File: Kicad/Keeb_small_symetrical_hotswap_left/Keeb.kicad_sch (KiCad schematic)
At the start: 28 parts, among them J1 TYPE-C-31-M-12, SW1 CherryMX, SW10 CherryMX, SW11 CherryMX, SW13 CherryMX, SW14 CherryMX, SW15 CherryMX, SW16 CherryMX, SW17 CherryMX, SW18 CherryMX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

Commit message: added encoder
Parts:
- added U2: KY-040, KY-040:KY-040-PORT, symbol KY-040:KY-040
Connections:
- net 28: now also U2.SW
- net 3: now also U2.DT
- net 3v3: now also J1.B5 (CC2), J1.B8 (SBU2), U2.VCC; no longer J1.A4_B9 (VBUS), J1.B4_A9 (VBUS)
- net 4: now also U2.CLK
- net GND: now also U2.GND
- net VSYS: now also J1.A4_B9 (VBUS), J1.B4_A9 (VBUS); no longer J1.B5 (CC2), J1.B8 (SBU2)

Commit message: Managed to add a button, optimised tracks, switched some connections around
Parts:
- added SW2: CherryMX, ScottoKeebs_Hotswap:Hotswap_MX_1.00u, symbol Keeb-rescue:CherryMX-CherryMX
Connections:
- net 0: no longer J1.A5 (CC1), J1.A8 (SBU1)
- net 1: now also SW2.2; no longer J1.A6 (DP1), J1.A7 (DN1)
- net 14: now also J1.A6 (DP1), J1.A7 (DN1)
- net 15: now also J1.B6 (DP2), J1.B7 (DN2)
- net 2: now also J1.A5 (CC1), J1.A8 (SBU1); no longer J1.B6 (DP2), J1.B7 (DN2)
- net 20: now also SW16.1; no longer SW15.2
- net 21: now also SW15.2; no longer SW19.1
- net 22: now also SW19.1; no longer SW20.1
- net 26: now also SW20.1; no longer SW16.1
- net GND: now also SW2.1
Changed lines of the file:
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@@
     (stroke (width 0) (type default))
   )
-  (global_label "26" (shape input) (at 146.05 97.79 270) (fields_autoplaced)
+  (global_label "20" (shape input) (at 146.05 97.79 270) (fields_autoplaced)
     (effects (font (size 1.27 1.27)) (justify right))
     (property "Intersheetrefs" "${INTERSHEET_REFS}" (at 146.05 102.54 90)
@@
     )
   )
-  (global_label "2" (shape input) (at 91.44 36.83 0) (fields_autoplaced)
-    (effects (font (size 1.27 1.27)) (justify left))
-    (property "Intersheetrefs" "${INTERSHEET_REFS}" (at 94.9805 36.83 0)
+  (global_label "15" (shape input) (at 91.44 36.83 0) (fields_autoplaced)
+    (effects (font (size 1.27 1.27)) (justify left))
+    (property "Intersheetrefs" "${INTERSHEET_REFS}" (at 96.19 36.83 0)
       (effects (font (size 1.27 1.27)) (justify left) hide)
     )
@@
     )
   )
-  (global_label "20" (shape input) (at 156.21 85.09 270) (fields_autoplaced)
+  (global_label "21" (shape input) (at 156.21 85.09 270) (fields_autoplaced)
     (effects (font (size 1.27 1.27)) (justify right))
     (property "Intersheetrefs" "${INTERSHEET_REFS}" (at 156.21 89.84 90)
@@
     )
   )
-  (global_label "1" (shape input) (at 48.26 36.83 180) (fields_autoplaced)
-    (effects (font (size 1.27 1.27)) (justify right))
-    (property "Intersheetrefs" "${INTERSHEET_REFS}" (at 44.7195 36.83 0)
+  (global_label "14" (shape input) (at 48.26 36.83 180) (fields_autoplaced)
+    (effects (font (size 1.27 1.27)) (justify right))
+    (property "Intersheetrefs" "${INTERSHEET_REFS}" (at 43.51 36.83 0)
       (effects (font (size 1.27 1.27)) (justify right) hide)
     )
@@
     )
   )
+  (global_label "GND" (shape input) (at 118.11 97.79 270) (fields_autoplaced)
+    (effects (font (size 1.27 1.27)) (justify right))
+    (property "Intersheetrefs" "${INTERSHEET_REFS}" (at 118.11 103.9915 90)
+      (effects (font (size 1.27 1.27)) (justify right) hide)
+    )
+  )
   (global_label "18" (shape input) (at 156.21 72.39 270) (fields_autoplaced)
     (effects (font (size 1.27 1.27)) (justify right))
@@
     )
   )
-  (global_label "21" (shape input) (at 158.75 85.09 270) (fields_autoplaced)
+  (global_label "22" (shape input) (at 158.75 85.09 270) (fields_autoplaced)
     (effects (font (size 1.27 1.27)) (justify right))
     (property "Intersheetrefs" "${INTERSHEET_REFS}" (at 158.75 89.84 90)
@@
     )
   )
+  (global_label "1" (shape input) (at 128.27 97.79 270) (fields_autoplaced)
+    (effects (font (size 1.27 1.27)) (justify right))
+    (property "Intersheetrefs" "${INTERSHEET_REFS}" (at 128.27 101.3305 90)
+      (effects (font (size 1.27 1.27)) (justify right) hide)
+    )
+  )
   (global_label "19" (shape input) (at 85.09 119.38 0) (fields_autoplaced)
     (effects (font (size 1.27 1.27)) (justify left))
@@
     )
   )
-  (global_label "22" (shape input) (at 158.75 97.79 90) (fields_autoplaced)
+  (global_label "26" (shape input) (at 158.75 97.79 90) (fields_autoplaced)
     (effects (font (size 1.27 1.27)) (justify left))
     (property "Intersheetrefs" "${INTERSHEET_REFS}" (at 158.75 93.04 90)
@@
     )
   )
-  (global_label "0" (shape input) (at 44.45 34.29 180) (fields_autoplaced)
+  (global_label "2" (shape input) (at 44.45 34.29 180) (fields_autoplaced)
     (effects (font (size 1.27 1.27)) (justify right))
     (property "Intersheetrefs" "${INTERSHEET_REFS}" (at 40.9095 34.29 0)
@@
         )
       )
+    )
+  )
+  (symbol (lib_id "Keeb-rescue:CherryMX-CherryMX") (at 123.19 97.79 0) (unit 1)
+    (in_bom yes) (on_board yes) (dnp no)
+    (property "Reference" "SW2" (at 123.19 90.551 0)
+      (effects (font (size 1.27 1.27)))
+    )
+    (property "Value" "CherryMX" (at 123.19 92.8624 0)
+      (effects (font (size 1.27 1.27)))
+    )
+    (property "Footprint" "ScottoKeebs_Hotswap:Hotswap_MX_1.00u" (at 123.19 97.155 0)
+      (effects (font (size 1.27 1.27)) hide)
+    )
+    (property "Datasheet" "" (at 123.19 97.155 0)
+      (effects (font (size 1.27 1.27)) hide)
+    )
+    (pin "1")
+    (pin "2")
+    (instances
+      (project "Keeb"
+        (path "/f8892ba2-997e-41dc-a7e4-c2b6962ff100"
+          (reference "SW2") (unit 1)
+        )
+      )

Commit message: Updated a PiPico footprint
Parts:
- U1: footprint MCU_RaspberryPi_and_Boards:RPi_Pico_SMD_TH_NO_HOLES -> MCU_RaspberryPi_and_Boards:RPi_Pico_SMD_TH_NO_BACK_HOLES
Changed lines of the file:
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@@
       (effects (font (size 1.27 1.27)))
     )
-    (property "Footprint" "MCU_RaspberryPi_and_Boards:RPi_Pico_SMD_TH_NO_HOLES" (at 67.31 105.41 90)
+    (property "Footprint" "MCU_RaspberryPi_and_Boards:RPi_Pico_SMD_TH_NO_BACK_HOLES" (at 67.31 105.41 90)
       (effects (font (size 1.27 1.27)) hide)
     )

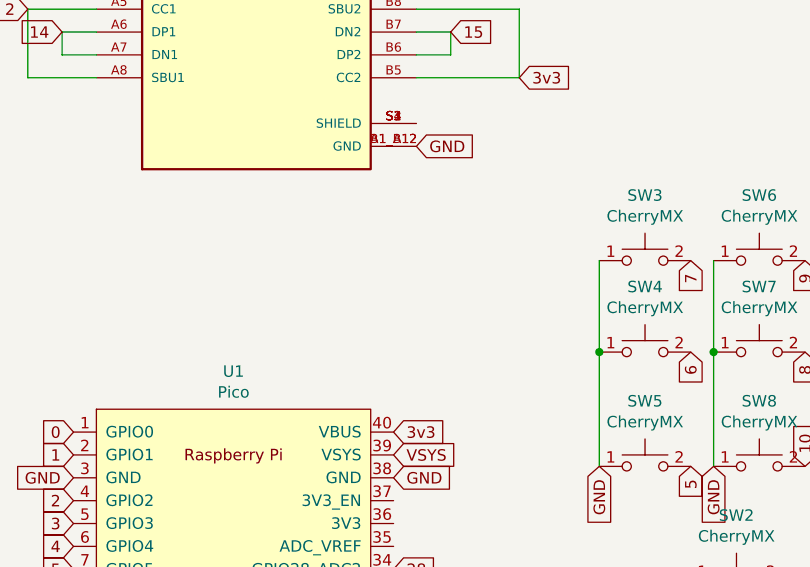
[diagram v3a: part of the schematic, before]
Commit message: added a connectior for the battery
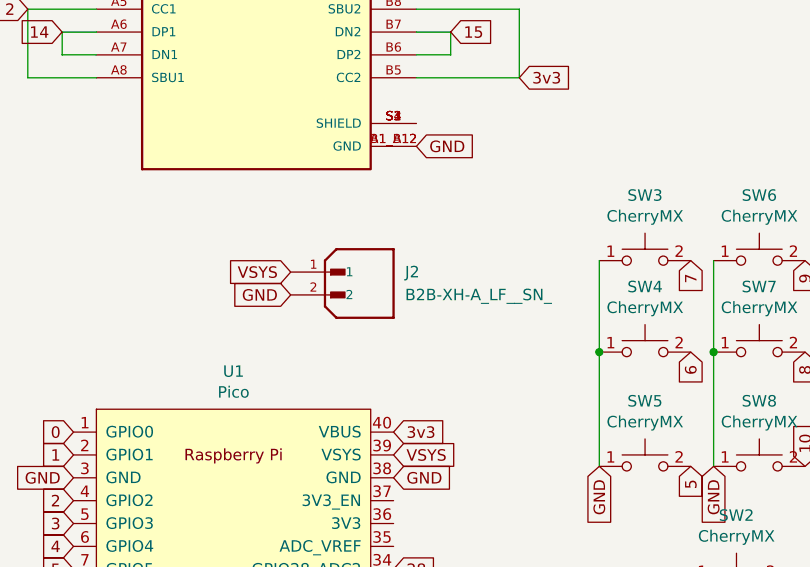
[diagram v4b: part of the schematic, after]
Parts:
- added J2: B2B-XH-A_LF__SN_, Connectors_user:JST_B2B-XH-A_LF__SN_, symbol B2B-XH-A_LF__SN_:B2B-XH-A_LF__SN_
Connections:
- net GND: now also J2.2
- net VSYS: now also J2.1
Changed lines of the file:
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@@
+    )
+  )
+  (global_label "GND" (shape input) (at 73.66 66.04 180) (fields_autoplaced)
+    (effects (font (size 1.27 1.27)) (justify right))
+    (property "Intersheetrefs" "${INTERSHEET_REFS}" (at 67.4585 66.04 0)
+      (effects (font (size 1.27 1.27)) (justify right) hide)
     )
   )
@@
     (effects (font (size 1.27 1.27)) (justify right))
     (property "Intersheetrefs" "${INTERSHEET_REFS}" (at 118.11 88.6305 90)
+      (effects (font (size 1.27 1.27)) (justify right) hide)
+    )
+  )
+  (global_label "VSYS" (shape input) (at 73.66 63.5 180) (fields_autoplaced)
+    (effects (font (size 1.27 1.27)) (justify right))
+    (property "Intersheetrefs" "${INTERSHEET_REFS}" (at 66.7328 63.5 0)
       (effects (font (size 1.27 1.27)) (justify right) hide)
     )
@@
         )
       )
+    )
+  )
+  (symbol (lib_id "B2B-XH-A_LF__SN_:B2B-XH-A_LF__SN_") (at 81.28 66.04 0) (unit 1)
+    (in_bom yes) (on_board yes) (dnp no) (fields_autoplaced)
+    (property "Reference" "J2" (at 86.36 63.5 0)
+      (effects (font (size 1.27 1.27)) (justify left))
+    )
+    (property "Value" "B2B-XH-A_LF__SN_" (at 86.36 66.04 0)
+      (effects (font (size 1.27 1.27)) (justify left))
+    )
+    (property "Footprint" "Connectors_user:JST_B2B-XH-A_LF__SN_" (at 81.28 66.04 0)
+      (effects (font (size 1.27 1.27)) (justify bottom) hide)
+    )
+    (property "Datasheet" "" (at 81.28 66.04 0)
+      (effects (font (size 1.27 1.27)) hide)
+    )
+    (property "MF" "JST Sales America Inc." (at 81.28 66.04 0)
+      (effects (font (size 1.27 1.27)) (justify bottom) hide)
+    )
+    (property "MAXIMUM_PACKAGE_HEIGHT" "7 mm" (at 81.28 66.04 0)
+      (effects (font (size 1.27 1.27)) (justify bottom) hide)
+    )
+    (property "Package" "None" (at 81.28 66.04 0)
+      (effects (font (size 1.27 1.27)) (justify bottom) hide)
+    )
+    (property "Price" "None" (at 81.28 66.04 0)
+      (effects (font (size 1.27 1.27)) (justify bottom) hide)
+    )
+    (property "Check_prices" "https://www.snapeda.com/parts/B2B-XH-A(LF)(SN)/JST+Sales+America+Inc./view-part/?ref=eda" (at 81.28 66.04 0)
+      (effects (font (size 1.27 1.27)) (justify bottom) hide)
+    )
+    (property "STANDARD" "Manufacturer Recommendations" (at 81.28 66.04 0)
+      (effects (font (size 1.27 1.27)) (justify bottom) hide)
+    )
+    (property "PARTREV" "N/A" (at 81.28 66.04 0)
+      (effects (font (size 1.27 1.27)) (justify bottom) hide)
+    )
+    (property "SnapEDA_Link" "https://www.snapeda.com/parts/B2B-XH-A(LF)(SN)/JST+Sales+America+Inc./view-part/?ref=snap" (at 81.28 66.04 0)
+      (effects (font (size 1.27 1.27)) (justify bottom) hide)
+    )
+    (property "MP" "B2B-XH-A(LF)(SN)" (at 81.28 66.04 0)
+      (effects (font (size 1.27 1.27)) (justify bottom) hide)
+    )
+    (property "Description" "\nConnector Header Through Hole 2 position 0.098 (2.50mm)\n" (at 81.28 66.04 0)
+      (effects (font (size 1.27 1.27)) (justify bottom) hide)
+    )
+    (property "Availability" "In Stock" (at 81.28 66.04 0)
+      (effects (font (size 1.27 1.27)) (justify bottom) hide)
+    )
+    (property "MANUFACTURER" "JST Sales America Inc." (at 81.28 66.04 0)
+      (effects (font (size 1.27 1.27)) (justify bottom) hide)
+    )
+    (pin "2")
+    (pin "1")
+    (instances
+      (project "Keeb"
+        (path "/f8892ba2-997e-41dc-a7e4-c2b6962ff100"
+          (reference "J2") (unit 1)
+        )
+      )

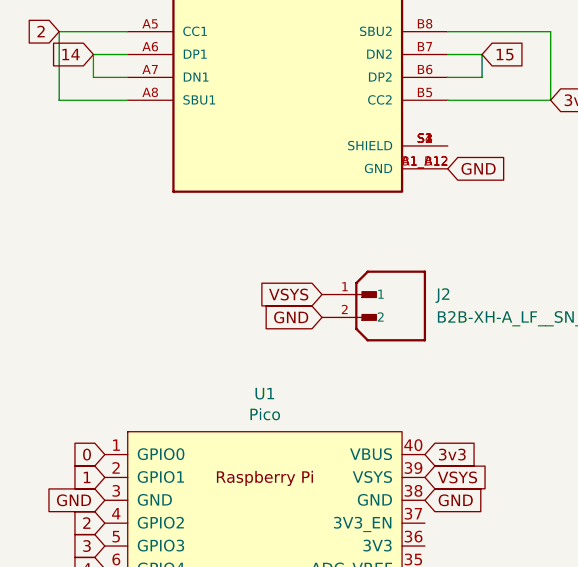
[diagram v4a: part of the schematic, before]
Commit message: added a on/off
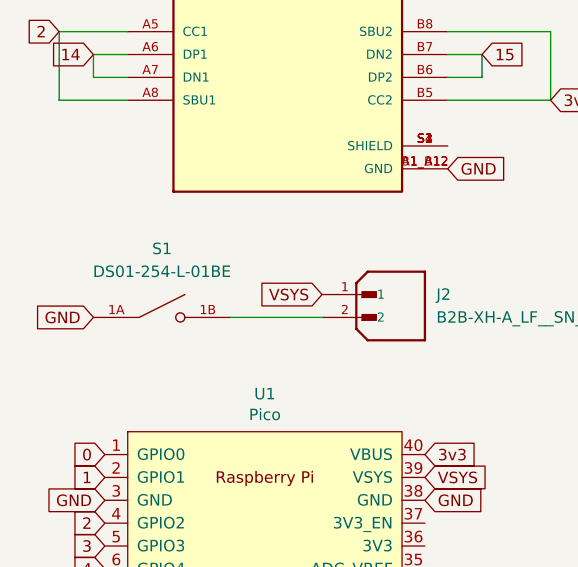
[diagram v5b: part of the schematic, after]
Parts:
- added S1: DS01-254-L-01BE, DIP:SW_DS01-254-L-01BE, symbol DS01-254-L-01BE:DS01-254-L-01BE
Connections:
- net GND: now also S1.1A; no longer J2.2
- new net: J2.2, S1.1B
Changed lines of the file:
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@@
+    (stroke (width 0) (type default))
+  )
+  (wire (pts (xy 63.5 66.04) (xy 73.66 66.04))
     (stroke (width 0) (type default))
   )
@@
     )
   )
+  (global_label "GND" (shape input) (at 48.26 66.04 180) (fields_autoplaced)
+    (effects (font (size 1.27 1.27)) (justify right))
+    (property "Intersheetrefs" "${INTERSHEET_REFS}" (at 42.0585 66.04 0)
+      (effects (font (size 1.27 1.27)) (justify right) hide)
+    )
+  )
   (global_label "19" (shape input) (at 156.21 62.23 270) (fields_autoplaced)
     (effects (font (size 1.27 1.27)) (justify right))
@@
     (effects (font (size 1.27 1.27)) (justify right))
     (property "Intersheetrefs" "${INTERSHEET_REFS}" (at 45.9895 101.6 0)
-      (effects (font (size 1.27 1.27)) (justify right) hide)
-    )
-  )
-  (global_label "GND" (shape input) (at 73.66 66.04 180) (fields_autoplaced)
-    (effects (font (size 1.27 1.27)) (justify right))
-    (property "Intersheetrefs" "${INTERSHEET_REFS}" (at 67.4585 66.04 0)
       (effects (font (size 1.27 1.27)) (justify right) hide)
     )
@@
         )
       )
+    )
+  )
+  (symbol (lib_id "DS01-254-L-01BE:DS01-254-L-01BE") (at 55.88 66.04 0) (unit 1)
+    (in_bom yes) (on_board yes) (dnp no) (fields_autoplaced)
+    (property "Reference" "S1" (at 55.88 58.42 0)
+      (effects (font (size 1.27 1.27)))
+    )
+    (property "Value" "DS01-254-L-01BE" (at 55.88 60.96 0)
+      (effects (font (size 1.27 1.27)))
+    )
+    (property "Footprint" "DIP:SW_DS01-254-L-01BE" (at 55.88 66.04 0)
+      (effects (font (size 1.27 1.27)) (justify bottom) hide)
+    )
+    (property "Datasheet" "" (at 55.88 66.04 0)
+      (effects (font (size 1.27 1.27)) hide)
+    )
+    (property "MF" "CUI Devices" (at 55.88 66.04 0)
+      (effects (font (size 1.27 1.27)) (justify bottom) hide)
+    )
+    (property "MAXIMUM_PACKAGE_HEIGHT" "7.0mm" (at 55.88 66.04 0)
+      (effects (font (size 1.27 1.27)) (justify bottom) hide)
+    )
+    (property "Package" "None" (at 55.88 66.04 0)
+      (effects (font (size 1.27 1.27)) (justify bottom) hide)
+    )
+    (property "Price" "None" (at 55.88 66.04 0)
+      (effects (font (size 1.27 1.27)) (justify bottom) hide)
+    )
+    (property "Check_prices" "https://www.snapeda.com/parts/DS01-254-L-01BE/CUI+Devices/view-part/?ref=eda" (at 55.88 66.04 0)
+      (effects (font (size 1.27 1.27)) (justify bottom) hide)
+    )
+    (property "STANDARD" "Manufacturer recommendations" (at 55.88 66.04 0)
+      (effects (font (size 1.27 1.27)) (justify bottom) hide)
+    )
+    (property "PARTREV" "1.0" (at 55.88 66.04 0)
+      (effects (font (size 1.27 1.27)) (justify bottom) hide)
+    )
+    (property "SnapEDA_Link" "https://www.snapeda.com/parts/DS01-254-L-01BE/CUI+Devices/view-part/?ref=snap" (at 55.88 66.04 0)
+      (effects (font (size 1.27 1.27)) (justify bottom) hide)
+    )
+    (property "MP" "DS01-254-L-01BE" (at 55.88 66.04 0)
+      (effects (font (size 1.27 1.27)) (justify bottom) hide)
+    )
+    (property "Purchase-URL" "https://www.snapeda.com/api/url_track_click_mouser/?unipart_id=4467329&manufacturer=CUI Devices&part_name=DS01-254-L-01BE&search_term=None" (at 55.88 66.04 0)
+      (effects (font (size 1.27 1.27)) (justify bottom) hide)
+    )
+    (property "Description" "1 Position, Through Hole, 2.54 mm Pitch, Raised Slide Actuator, Flat Bottom, Long Pin, DIP Switch" (at 55.88 66.04 0)
+      (effects (font (size 1.27 1.27)) (justify bottom) hide)
+    )
+    (property "CUI_purchase_URL" "https://www.cuidevices.com/product/switches/dip-switches/ds01-254-l-01be?utm_source=snapeda.com&utm_medium=referral&utm_campaign=snapedaBOM" (at 55.88 66.04 0)
+      (effects (font (size 1.27 1.27)) (justify bottom) hide)
+    )
+    (property "Availability" "In Stock" (at 55.88 66.04 0)
+      (effects (font (size 1.27 1.27)) (justify bottom) hide)
+    )
+    (property "MANUFACTURER" "CUI" (at 55.88 66.04 0)
+      (effects (font (size 1.27 1.27)) (justify bottom) hide)
+    )
+    (pin "1A")
+    (pin "1B")
+    (instances
+      (project "Keeb"
+        (path "/f8892ba2-997e-41dc-a7e4-c2b6962ff100"
+          (reference "S1") (unit 1)
+        )
+      )
